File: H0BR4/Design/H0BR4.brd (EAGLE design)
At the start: 34.6 x 30 mm, 26 parts, among them P1 HEXABIT_17.32, U1 STM32G0B1CEU6N, U2 LSM6DS3TR-C, U3 STMICROELECTRONICS_LSM303AGRT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, X1 CSTNE8M00G550000R0

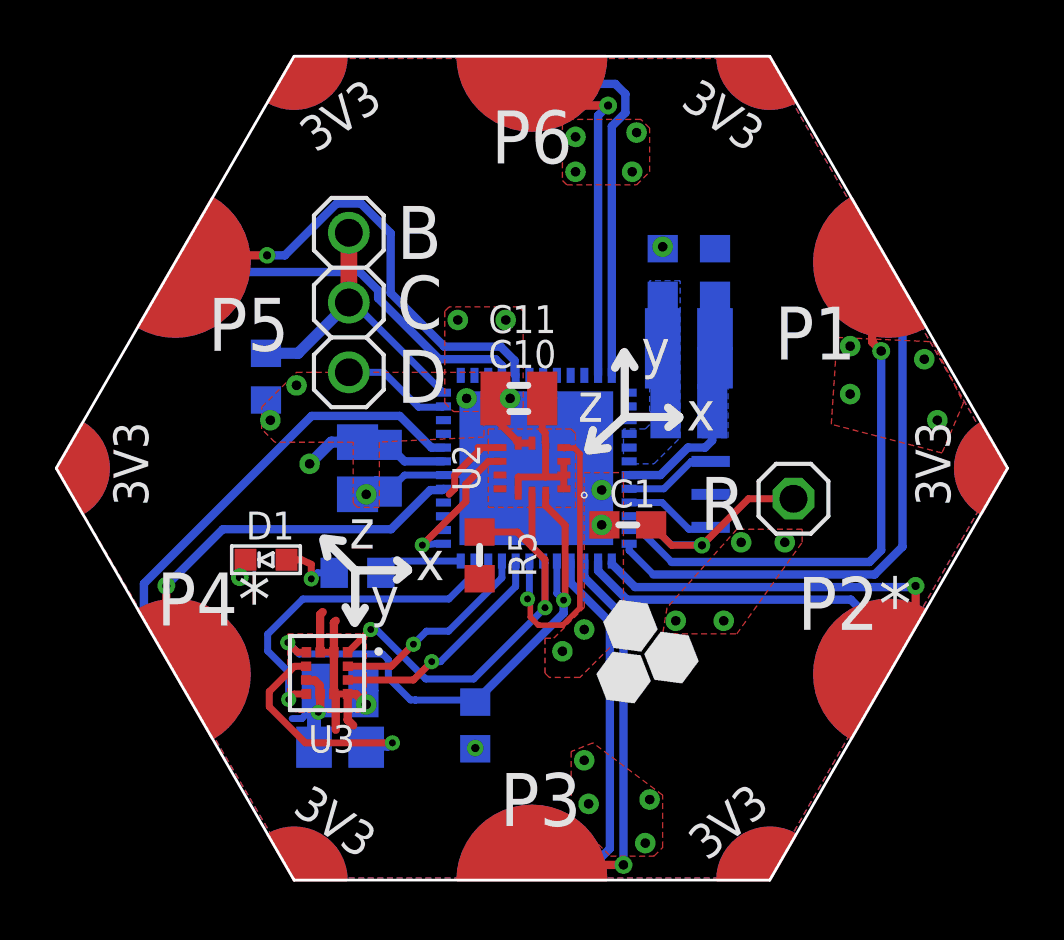
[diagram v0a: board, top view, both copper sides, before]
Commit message: update the logo add TVS
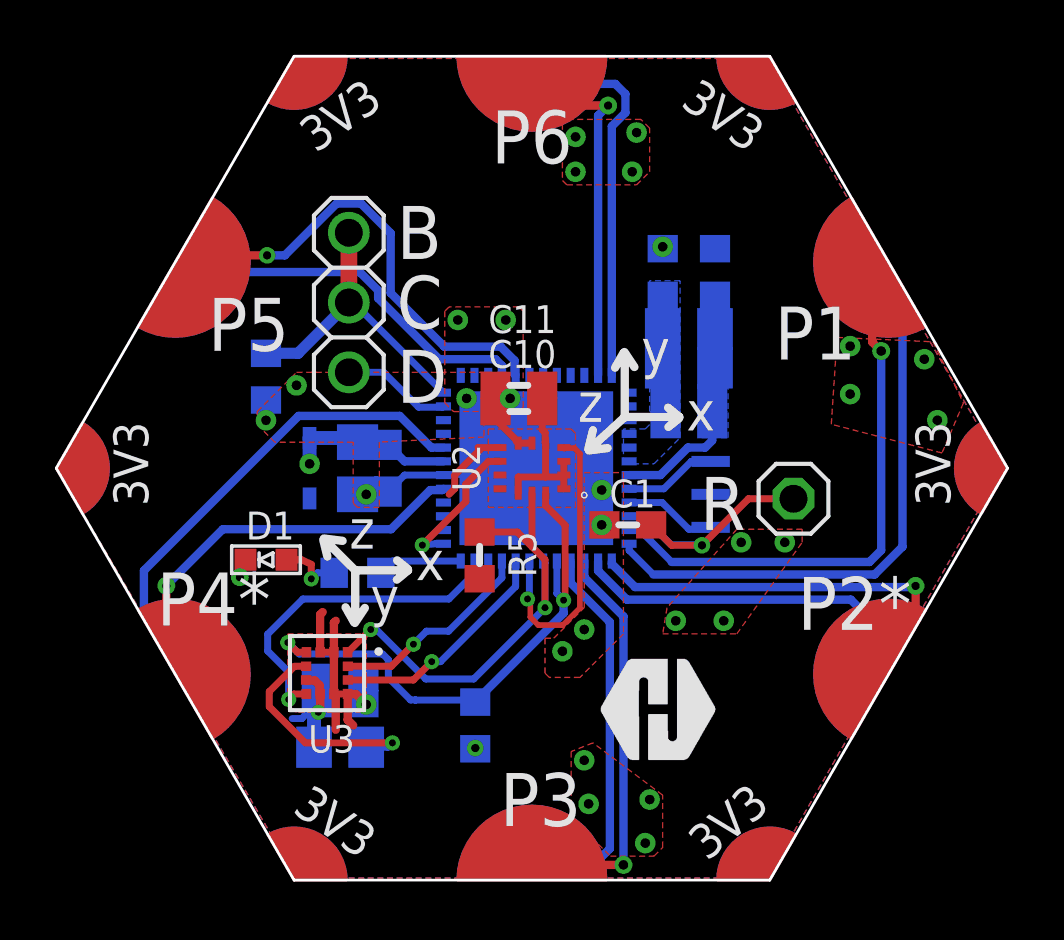
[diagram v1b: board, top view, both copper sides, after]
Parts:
- added D2: BOURNS_CDSOD323-T03SCBOURNS_CDSOD323-T03SC_0_0, HEXABITZ_RCLS:BOURNS_CDSOD323-T03SC_0
- added TRIMBLE-LOGO1: HEXA-LOGO, HEXABITZ_USER_INTERFACE_PARTS:HEXA-LOGO
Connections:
- net GND: now also D2.1
- net VDD: now also D2.2
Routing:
- net VDD: track 24.9 -> 25.6 mm
